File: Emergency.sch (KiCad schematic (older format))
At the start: 19 parts, among them J31 EMERGENCY, J32 EPSON POWER IN, J33 EPSON BOARD POWER, K1 S13-24V-2C, Q17 BC817, U10 74HC2G32

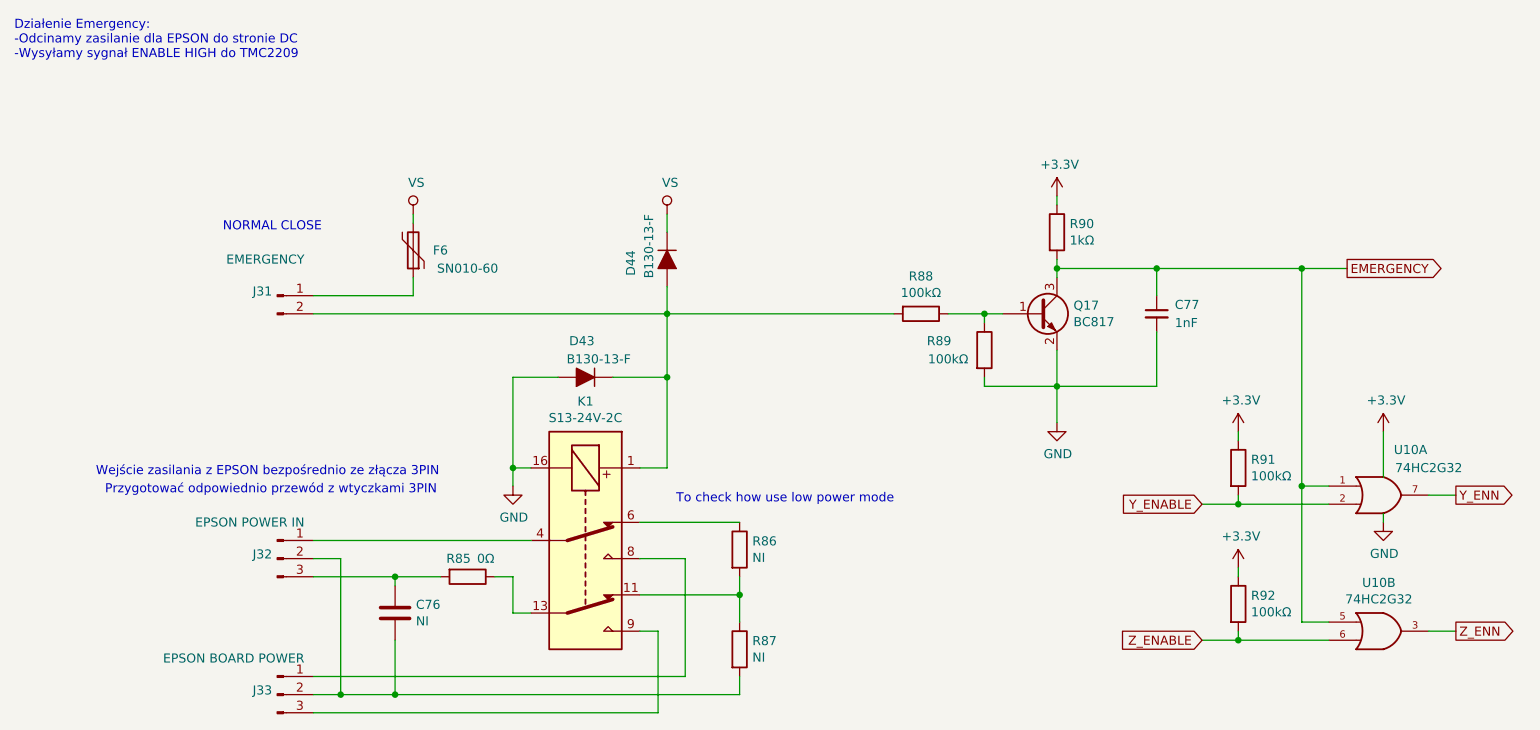
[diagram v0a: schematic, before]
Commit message: Improve ESD Protection for TMC2209, Fuses. Schematic ready v1
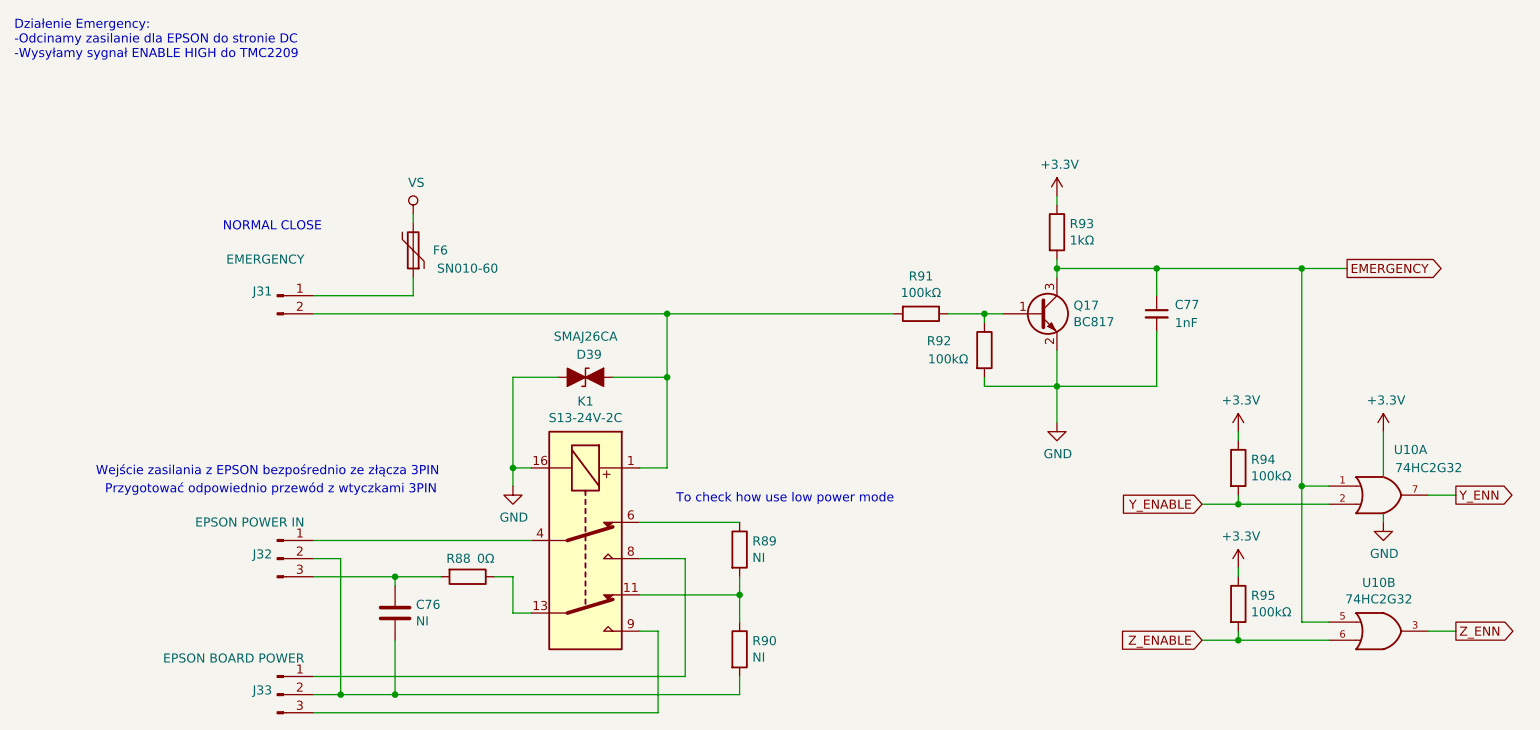
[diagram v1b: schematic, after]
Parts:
- removed D43, D44: B130-13-F, Diode_SMD:D_SMA, symbol Device:D_ALT
- added D39: SMAJ26CA, Diode_SMD:D_SMA, symbol Device:D_TVS_ALT
- renumbered R85 to R88, R86 to R89, R87 to R90, R88 to R91, R89 to R92, R90 to R93, R91 to R94, R92 to R95
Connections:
- net GND: now also D39.1 (A1)
- net at J31.2 (Pin_2), K1.1, R91.2: now also D39.2 (A2)
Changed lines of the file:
@@
 	4500 3200 4350 3200
 $Comp
-L power:GND #PWR0182
+L power:GND #PWR0174
 U 1 1 5E128738
 P 3650 3300
-F 0 "#PWR0182" H 3650 3050 50  0001 C CNN
+F 0 "#PWR0174" H 3650 3050 50  0001 C CNN
 F 1 "GND" H 3655 3127 50  0000 C CNN
 F 2 "" H 3650 3300 50  0001 C CNN
@@
 Connection ~ 3650 3200
 $Comp
-L Device:R R88
+L Device:R R91
 U 1 1 5E137914
 P 5900 2350
-F 0 "R88" V 5693 2350 50  0000 C CNN
+F 0 "R91" V 5693 2350 50  0000 C CNN
 F 1 "100kΩ" V 5784 2350 50  0000 C CNN
 F 2 "Resistor_SMD:R_0603_1608Metric" V 5830 2350 50  0001 C CNN
@@
 $EndComp
 $Comp
-L power:GND #PWR0185
+L power:GND #PWR0176
 U 1 1 5E13A402
 P 6650 2950
-F 0 "#PWR0185" H 6650 2700 50  0001 C CNN
+F 0 "#PWR0176" H 6650 2700 50  0001 C CNN
 F 1 "GND" H 6655 2777 50  0000 C CNN
 F 2 "" H 6650 2950 50  0001 C CNN
@@
 	6650 2550 6650 2750
 $Comp
-L Device:R R90
+L Device:R R93
 U 1 1 5E13AACA
 P 6650 1900
-F 0 "R90" H 6720 1946 50  0000 L CNN
+F 0 "R93" H 6720 1946 50  0000 L CNN
 F 1 "1kΩ" H 6720 1855 50  0000 L CNN
 F 2 "Resistor_SMD:R_0603_1608Metric" V 6580 1900 50  0001 C CNN
@@
 	6650 1700 6650 1750
 $Comp
-L power:+3.3V #PWR0184
+L power:+3.3V #PWR0175
 U 1 1 5E13B5C9
 P 6650 1700
-F 0 "#PWR0184" H 6650 1550 50  0001 C CNN
+F 0 "#PWR0175" H 6650 1550 50  0001 C CNN
 F 1 "+3.3V" H 6665 1873 50  0000 C CNN
 F 2 "" H 6650 1700 50  0001 C CNN
@@
 $EndComp
 $Comp
-L power:GND #PWR0189
+L power:GND #PWR0180
 U 1 1 5E136188
 P 8450 3500
-F 0 "#PWR0189" H 8450 3250 50  0001 C CNN
+F 0 "#PWR0180" H 8450 3250 50  0001 C CNN
 F 1 "GND" H 8455 3327 50  0000 C CNN
 F 2 "" H 8450 3500 50  0001 C CNN
@@
 $EndComp
 $Comp
-L power:+3.3V #PWR0188
+L power:+3.3V #PWR0179
 U 1 1 5E13670F
 P 8450 3000
-F 0 "#PWR0188" H 8450 2850 50  0001 C CNN
+F 0 "#PWR0179" H 8450 2850 50  0001 C CNN
 F 1 "+3.3V" H 8465 3173 50  0000 C CNN
 F 2 "" H 8450 3000 50  0001 C CNN
@@
 	7450 4150 7650 4150
 $Comp
-L Device:R R92
+L Device:R R95
 U 1 1 5E14A9EB
 P 7650 3950
-F 0 "R92" H 7720 3996 50  0000 L CNN
+F 0 "R95" H 7720 3996 50  0000 L CNN
 F 1 "100kΩ" H 7720 3905 50  0000 L CNN
 F 2 "Resistor_SMD:R_0603_1608Metric" V 7580 3950 50  0001 C CNN
@@
 	6650 2100 6650 2150
 $Comp
-L Device:R R91
+L Device:R R94
 U 1 1 5E14F006
 P 7650 3200
-F 0 "R91" H 7720 3246 50  0000 L CNN
+F 0 "R94" H 7720 3246 50  0000 L CNN
 F 1 "100kΩ" H 7720 3155 50  0000 L CNN
 F 2 "Resistor_SMD:R_0603_1608Metric" V 7580 3200 50  0001 C CNN
@@
 	7650 3400 7450 3400
 $Comp
-L power:+3.3V #PWR0186
+L power:+3.3V #PWR0177
 U 1 1 5E151EAA
 P 7650 3000
-F 0 "#PWR0186" H 7650 2850 50  0001 C CNN
+F 0 "#PWR0177" H 7650 2850 50  0001 C CNN
 F 1 "+3.3V" H 7665 3173 50  0000 C CNN
 F 2 "" H 7650 3000 50  0001 C CNN
@@
 $EndComp
 $Comp
-L power:+3.3V #PWR0187
+L power:+3.3V #PWR0178
 U 1 1 5E152501
 P 7650 3750
-F 0 "#PWR0187" H 7650 3600 50  0001 C CNN
+F 0 "#PWR0178" H 7650 3600 50  0001 C CNN
 F 1 "+3.3V" H 7665 3923 50  0000 C CNN
 F 2 "" H 7650 3750 50  0001 C CNN
@@
 Wire Wire Line
 	6650 2750 6650 2950
-$Comp
-L Device:D_ALT D?
-U 1 1 5E199862
-P 4050 2700
-AR Path="/5E1018C2/5E199862" Ref="D?"  Part="1"
-AR Path="/5E91D7CC/5E199862" Ref="D43"  Part="1"
-F 0 "D43" H 4000 2500 50  0000 L CNN
-F 1 "B130-13-F" H 3800 2600 50  0000 L CNN
-F 2 "Diode_SMD:D_SMA" H 4050 2700 50  0001 C CNN
-F 3 "~" H 4050 2700 50  0001 C CNN
-F 4 "0.29301" H 4050 2700 50  0001 C CNN "Cena"
-F 5 "https://www.tme.eu/pl/details/b130-13-f/diody-schottky-smd/diodes-incorporated/" H 4050 2700 50  0001 C CNN "Link"
-F 6 "B130-13-F" H 4050 2700 50  0001 C CNN "Model"
-F 7 "Dioda: prostownicza Schottky; SMD; 40V; 1A; SMA" H 4050 2700 50  0001 C CNN "Opis"
-F 8 "DIODES INCORPORATED" H 4050 2700 50  0001 C CNN "Producent"
-F 9 "SMD" H 4050 2700 50  0001 C CNN "Typ"
-	1    4050 2700
-	-1   0    0    1
-$EndComp
 Wire Wire Line
 	4500 2350 5750 2350
 $Comp
-L Device:D_ALT D?
-U 1 1 5E28E0C0
-P 4500 2050
-AR Path="/5E1018C2/5E28E0C0" Ref="D?"  Part="1"
-AR Path="/5E91D7CC/5E28E0C0" Ref="D44"  Part="1"
-F 0 "D44" H 4450 1850 50  0000 L CNN
-F 1 "B130-13-F" H 4250 1950 50  0000 L CNN
-F 2 "Diode_SMD:D_SMA" H 4500 2050 50  0001 C CNN
-F 3 "~" H 4500 2050 50  0001 C CNN
-F 4 "0.29301" H 4500 2050 50  0001 C CNN "Cena"
-F 5 "https://www.tme.eu/pl/details/b130-13-f/diody-schottky-smd/diodes-incorporated/" H 4500 2050 50  0001 C CNN "Link"
-F 6 "B130-13-F" H 4500 2050 50  0001 C CNN "Model"
-F 7 "Dioda: prostownicza Schottky; SMD; 40V; 1A; SMA" H 4500 2050 50  0001 C CNN "Opis"
-F 8 "DIODES INCORPORATED" H 4500 2050 50  0001 C CNN "Producent"
-F 9 "SMD" H 4500 2050 50  0001 C CNN "Typ"
-	1    4500 2050
-	0    1    1    0
-$EndComp
-$Comp
-L power:VS #PWR?
-U 1 1 5E28EAC8
-P 4500 1800
-AR Path="/5E1018C2/5E28EAC8" Ref="#PWR?"  Part="1"
-AR Path="/5E91D7CC/5E28EAC8" Ref="#PWR0183"  Part="1"
-F 0 "#PWR0183" H 4300 1650 50  0001 C CNN
-F 1 "VS" H 4517 1973 50  0000 C CNN
-F 2 "" H 4500 1800 50  0001 C CNN
-F 3 "" H 4500 1800 50  0001 C CNN
-	1    4500 1800
-	1    0    0    -1
-$EndComp
-Wire Wire Line
-	4500 1800 4500 1900
-Wire Wire Line
-	4500 2200 4500 2350
-$Comp
-L Device:R R86
+L Device:R R89
 U 1 1 5E291C98
 P 4900 3650
-F 0 "R86" H 4970 3696 50  0000 L CNN
+F 0 "R89" H 4970 3696 50  0000 L CNN
 F 1 "NI" H 4970 3605 50  0000 L CNN
 F 2 "Resistor_SMD:R_0805_2012Metric" V 4830 3650 50  0001 C CNN
@@
 $EndComp
 $Comp
-L Device:R R87
+L Device:R R90
 U 1 1 5E292A48
 P 4900 4200
-F 0 "R87" H 4970 4246 50  0000 L CNN
+F 0 "R90" H 4970 4246 50  0000 L CNN
 F 1 "NI" H 4970 4155 50  0000 L CNN
 F 2 "Resistor_SMD:R_0805_2012Metric" V 4830 4200 50  0001 C CNN
@@
 To check how use low power mode
 $Comp
-L Device:R R85
+L Device:R R88
 U 1 1 5E297579
 P 3400 3800
-F 0 "R85" V 3300 3750 50  0000 C CNN
+F 0 "R88" V 3300 3750 50  0000 C CNN
 F 1 "0Ω" V 3300 3900 50  0000 C CNN
 F 2 "Resistor_SMD:R_0805_2012Metric" V 3330 3800 50  0001 C CNN
@@
 	3000 3800 3250 3800
 $Comp
-L Device:R R89
+L Device:R R92
 U 1 1 5E48FDB2
 P 6250 2550
-F 0 "R89" H 6000 2600 50  0000 C CNN
+F 0 "R92" H 6000 2600 50  0000 C CNN
 F 1 "100kΩ" H 6050 2500 50  0000 C CNN
 F 2 "Resistor_SMD:R_0603_1608Metric" V 6180 2550 50  0001 C CNN
@@
 P 3100 1800
 AR Path="/5E1018C2/5E40B316" Ref="#PWR?"  Part="1"
-AR Path="/5E91D7CC/5E40B316" Ref="#PWR0181"  Part="1"
-F 0 "#PWR0181" H 2900 1650 50  0001 C CNN
+AR Path="/5E91D7CC/5E40B316" Ref="#PWR0173"  Part="1"
+F 0 "#PWR0173" H 2900 1650 50  0001 C CNN
 F 1 "VS" H 3117 1973 50  0000 C CNN
 F 2 "" H 3100 1800 50  0001 C CNN
@@
 	1    0    0    -1
 $EndComp
+$Comp
+L Device:D_TVS_ALT D?
+U 1 1 5E295142
+P 4050 2700
+AR Path="/5DE587B9/5E295142" Ref="D?"  Part="1"
+AR Path="/5E91D7CC/5E295142" Ref="D39"  Part="1"
+F 0 "D39" H 4000 2825 50  0000 L CNN
+F 1 "SMAJ26CA" H 3875 2925 50  0000 L CNN
+F 2 "Diode_SMD:D_SMA" H 4050 2700 50  0001 C CNN
+F 3 "~" H 4050 2700 50  0001 C CNN
+F 4 "0.30" H 4050 2700 50  0001 C CNN "Cena"
+F 5 "https://www.tme.eu/pl/details/smaj26ca-tr/diody-transil-smd-dwukierunkowe/stmicroelectronics/smaj26ca/" H 4050 2700 50  0001 C CNN "Link"
+F 6 "26V" H 4050 2700 50  0001 C CNN "Napięcie"
+F 7 "Dioda: transil; 400W; 28,9V; 43A; dwukierunkowa; SMA" H 4050 2700 50  0001 C CNN "Opis"
+F 8 "STM" H 4050 2700 50  0001 C CNN "Producent"
+F 9 "SMD" H 4050 2700 50  0001 C CNN "Typ"
+	1    4050 2700
+	1    0    0    -1
+$EndComp

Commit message: TMC2209 routing step 2/3
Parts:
- added R46: 10Ω, Resistor_SMD:R_0603_1608Metric, symbol Device:R
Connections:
- net +3V3: now also R46.1; no longer U10.8 (VCC), U10.8 (VCC)
- new net VCC: R46.2, U10.8 (VCC), U10.8 (VCC)
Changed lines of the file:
@@
 L power:+3.3V #PWR0179
 U 1 1 5E13670F
-P 8450 3000
-F 0 "#PWR0179" H 8450 2850 50  0001 C CNN
-F 1 "+3.3V" H 8465 3173 50  0000 C CNN
-F 2 "" H 8450 3000 50  0001 C CNN
-F 3 "" H 8450 3000 50  0001 C CNN
-	1    8450 3000
-	1    0    0    -1
-$EndComp
-Wire Wire Line
-	8450 3000 8450 3250
+P 8450 2650
+F 0 "#PWR0179" H 8450 2500 50  0001 C CNN
+F 1 "+3.3V" H 8465 2823 50  0000 C CNN
+F 2 "" H 8450 2650 50  0001 C CNN
+F 3 "" H 8450 2650 50  0001 C CNN
+	1    8450 2650
+	1    0    0    -1
+$EndComp
+Wire Wire Line
+	8450 2650 8450 2750
 Wire Wire Line
 	8450 3450 8450 3500
@@
 	1    0    0    -1
 $EndComp
+$Comp
+L Device:R R46
+U 1 1 5E3EE5FF
+P 8450 2900
+F 0 "R46" H 8520 2946 50  0000 L CNN
+F 1 "10Ω" H 8520 2855 50  0000 L CNN
+F 2 "Resistor_SMD:R_0603_1608Metric" V 8380 2900 50  0001 C CNN
+F 3 "~" H 8450 2900 50  0001 C CNN
+F 4 "0.04651" H 8450 2900 50  0001 C CNN "Cena"
+F 5 "SMD" H 8450 2900 50  0001 C CNN "Typ"
+	1    8450 2900
+	1    0    0    -1
+$EndComp
+Wire Wire Line
+	8450 3050 8450 3250
 $EndSCHEMATC

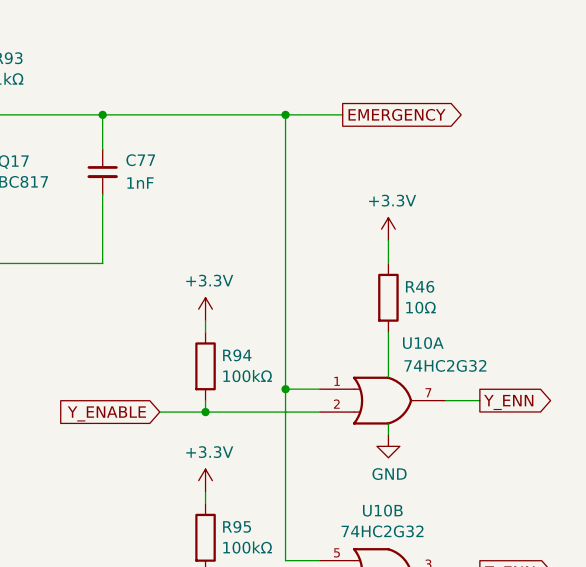
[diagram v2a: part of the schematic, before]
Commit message: Test points, start power plane routing, little change on schematic
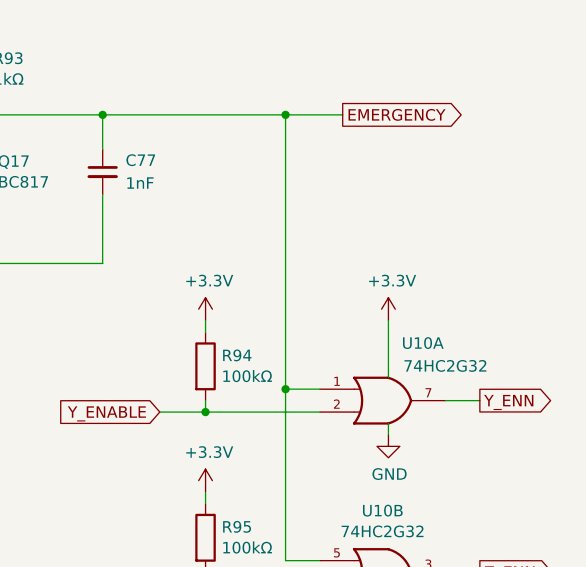
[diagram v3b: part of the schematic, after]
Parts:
- removed R46: 10Ω, Resistor_SMD:R_0603_1608Metric, symbol Device:R
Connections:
- net VCC is gone; now on net +3V3: U10.8 (VCC), U10.8 (VCC)
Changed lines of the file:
@@
 L power:+3.3V #PWR0179
 U 1 1 5E13670F
-P 8450 2650
-F 0 "#PWR0179" H 8450 2500 50  0001 C CNN
-F 1 "+3.3V" H 8465 2823 50  0000 C CNN
-F 2 "" H 8450 2650 50  0001 C CNN
-F 3 "" H 8450 2650 50  0001 C CNN
-	1    8450 2650
-	1    0    0    -1
-$EndComp
-Wire Wire Line
-	8450 2650 8450 2750
+P 8450 3000
+F 0 "#PWR0179" H 8450 2850 50  0001 C CNN
+F 1 "+3.3V" H 8465 3173 50  0000 C CNN
+F 2 "" H 8450 3000 50  0001 C CNN
+F 3 "" H 8450 3000 50  0001 C CNN
+	1    8450 3000
+	1    0    0    -1
+$EndComp
 Wire Wire Line
 	8450 3450 8450 3500
@@
 	1    0    0    -1
 $EndComp
-$Comp
-L Device:R R46
-U 1 1 5E3EE5FF
-P 8450 2900
-F 0 "R46" H 8520 2946 50  0000 L CNN
-F 1 "10Ω" H 8520 2855 50  0000 L CNN
-F 2 "Resistor_SMD:R_0603_1608Metric" V 8380 2900 50  0001 C CNN
-F 3 "~" H 8450 2900 50  0001 C CNN
-F 4 "0.04651" H 8450 2900 50  0001 C CNN "Cena"
-F 5 "SMD" H 8450 2900 50  0001 C CNN "Typ"
-	1    8450 2900
-	1    0    0    -1
-$EndComp
-Wire Wire Line
-	8450 3050 8450 3250
+Wire Wire Line
+	8450 3000 8450 3250
 $EndSCHEMATC

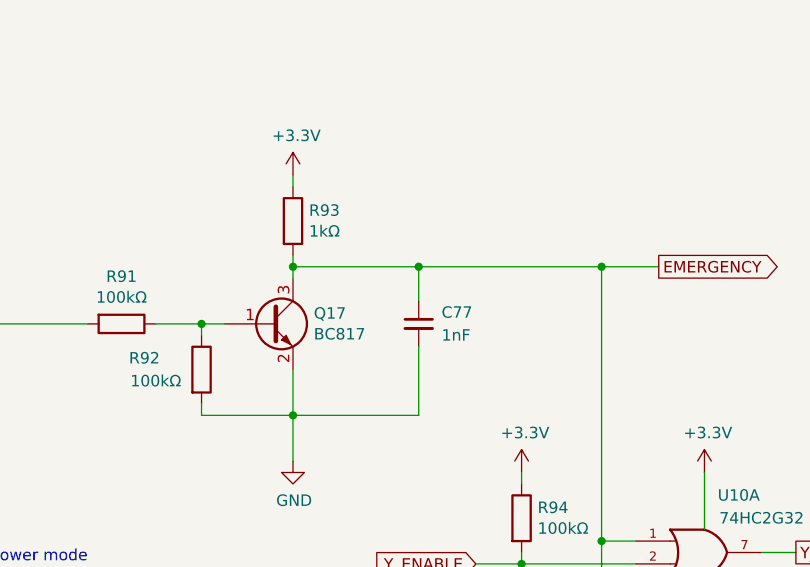
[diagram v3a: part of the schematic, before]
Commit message: Update elements value
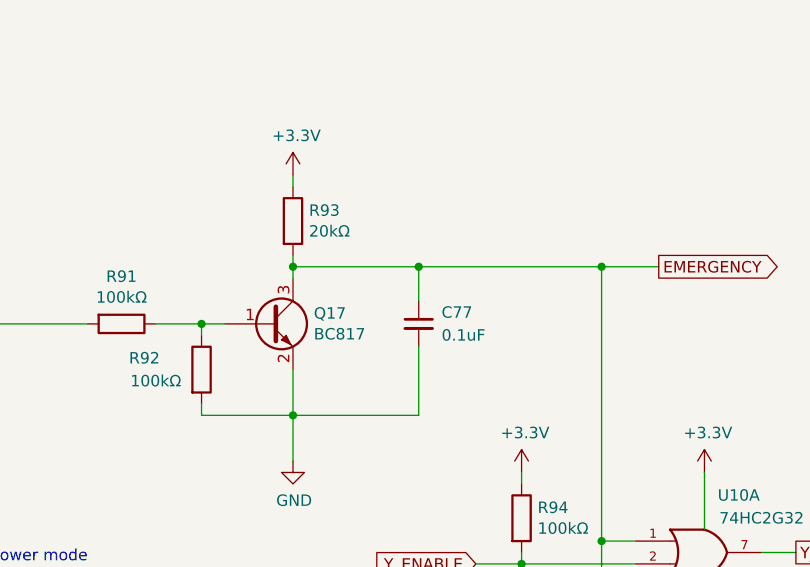
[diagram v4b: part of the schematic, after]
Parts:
- C76: Typ (none) -> SMD
- C77: value 1nF -> 0.1uF
- R93: value 1kΩ -> 20kΩ
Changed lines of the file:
@@
 P 6650 1900
 F 0 "R93" H 6720 1946 50  0000 L CNN
-F 1 "1kΩ" H 6720 1855 50  0000 L CNN
+F 1 "20kΩ" H 6720 1855 50  0000 L CNN
 F 2 "Resistor_SMD:R_0603_1608Metric" V 6580 1900 50  0001 C CNN
 F 3 "~" H 6650 1900 50  0001 C CNN
@@
 AR Path="/5E91D7CC/5E16709A" Ref="C77"  Part="1"
 F 0 "C77" H 7300 2400 50  0000 L CNN
-F 1 "1nF" H 7300 2300 50  0000 L CNN
+F 1 "0.1uF" H 7300 2300 50  0000 L CNN
 F 2 "Capacitor_SMD:C_0603_1608Metric" H 7200 2350 50  0001 C CNN
 F 3 "~" H 7200 2350 50  0001 C CNN
@@
 F 2 "Capacitor_SMD:C_0805_2012Metric" H 3038 3850 50  0001 C CNN
 F 3 "~" H 3000 4000 50  0001 C CNN
+F 4 "SMD" H 3000 4000 50  0001 C CNN "Typ"
 	1    3000 4000
 	1    0    0    -1
